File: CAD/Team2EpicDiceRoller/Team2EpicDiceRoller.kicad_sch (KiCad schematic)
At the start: 75 parts, among them J1 Conn_02x03_Odd_Even, J2 Conn_01x16, J3 Barrel_Jack, Q1 BSS138, SW1 SW_Toggle_SPDT, SW2 Tilt_Switch, SW3 SW_Power, SW4 RotaryEncoder_Switch, SW5 SW_LeftMenu, SW6 SW_MidMenu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

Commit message: updated layout, footprints look good
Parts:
- R12, R13: footprint Resistor_SMD:R_1206_3216Metric_Pad1.30x1.75mm_HandSolder -> Resistor_SMD:R_2512_6332Metric_Pad1.40x3.35mm_HandSolder
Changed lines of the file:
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@@
       (effects (font (size 1.27 1.27)) (justify left))
     )
-    (property "Footprint" "Resistor_SMD:R_1206_3216Metric_Pad1.30x1.75mm_HandSolder" (id 2) (at 153.162 179.07 90)
+    (property "Footprint" "Resistor_SMD:R_2512_6332Metric_Pad1.40x3.35mm_HandSolder" (id 2) (at 153.162 179.07 90)
       (effects (font (size 1.27 1.27)) hide)
     )
@@
       (effects (font (size 1.27 1.27)) (justify left))
     )
-    (property "Footprint" "Resistor_SMD:R_1206_3216Metric_Pad1.30x1.75mm_HandSolder" (id 2) (at 154.432 142.24 90)
+    (property "Footprint" "Resistor_SMD:R_2512_6332Metric_Pad1.40x3.35mm_HandSolder" (id 2) (at 154.432 142.24 90)
       (effects (font (size 1.27 1.27)) hide)
     )
@@
     )
     (path "/6b508d04-a0ae-4129-b291-a30a6f3fd6be"
-      (reference "R12") (unit 1) (value "150") (footprint "Resistor_SMD:R_1206_3216Metric_Pad1.30x1.75mm_HandSolder")
+      (reference "R12") (unit 1) (value "150") (footprint "Resistor_SMD:R_2512_6332Metric_Pad1.40x3.35mm_HandSolder")
     )
     (path "/889f4fab-9685-4cef-a698-9695691b09ce"
-      (reference "R13") (unit 1) (value "150") (footprint "Resistor_SMD:R_1206_3216Metric_Pad1.30x1.75mm_HandSolder")
+      (reference "R13") (unit 1) (value "150") (footprint "Resistor_SMD:R_2512_6332Metric_Pad1.40x3.35mm_HandSolder")
     )
     (path "/a2c9735e-4a2d-405c-869d-3d050fdc7cf6"

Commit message: Replaced footprint for 470uF cap
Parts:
- C6, C8: footprint Capacitor_THT:CP_Radial_D5.0mm_P2.50mm -> Capacitor_THT:CP_Radial_D6.3mm_P2.50mm
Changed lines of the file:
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@@
       (effects (font (size 1.27 1.27)) (justify left))
     )
-    (property "Footprint" "Capacitor_THT:CP_Radial_D5.0mm_P2.50mm" (id 2) (at 98.7552 173.99 0)
+    (property "Footprint" "Capacitor_THT:CP_Radial_D6.3mm_P2.50mm" (id 2) (at 98.7552 173.99 0)
       (effects (font (size 1.27 1.27)) hide)
     )
@@
       (effects (font (size 1.27 1.27)) (justify left))
     )
-    (property "Footprint" "Capacitor_THT:CP_Radial_D5.0mm_P2.50mm" (id 2) (at 129.2352 137.16 0)
+    (property "Footprint" "Capacitor_THT:CP_Radial_D6.3mm_P2.50mm" (id 2) (at 129.2352 137.16 0)
       (effects (font (size 1.27 1.27)) hide)
     )
@@
     )
     (path "/5742b5fd-3f8d-4d64-bb1a-04db38f14d1d"
-      (reference "C6") (unit 1) (value "470u") (footprint "Capacitor_THT:CP_Radial_D5.0mm_P2.50mm")
+      (reference "C6") (unit 1) (value "470u") (footprint "Capacitor_THT:CP_Radial_D6.3mm_P2.50mm")
     )
     (path "/e430aba8-016f-47fe-86d9-c150d7f518cd"
@@
     )
     (path "/9c48a684-ed08-4a42-8221-2c4c4eaf77cd"
-      (reference "C8") (unit 1) (value "470u") (footprint "Capacitor_THT:CP_Radial_D5.0mm_P2.50mm")
+      (reference "C8") (unit 1) (value "470u") (footprint "Capacitor_THT:CP_Radial_D6.3mm_P2.50mm")
     )
     (path "/7e5013ac-be8e-44d0-99da-910d44977e25"

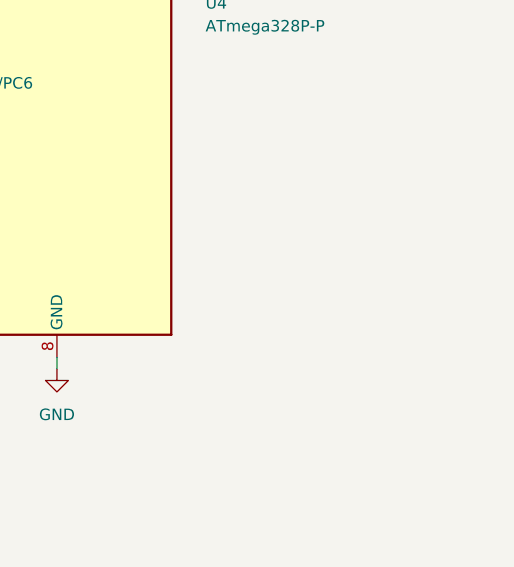
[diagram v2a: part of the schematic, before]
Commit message: Added mounting holes, updated general layout of pcb for routing
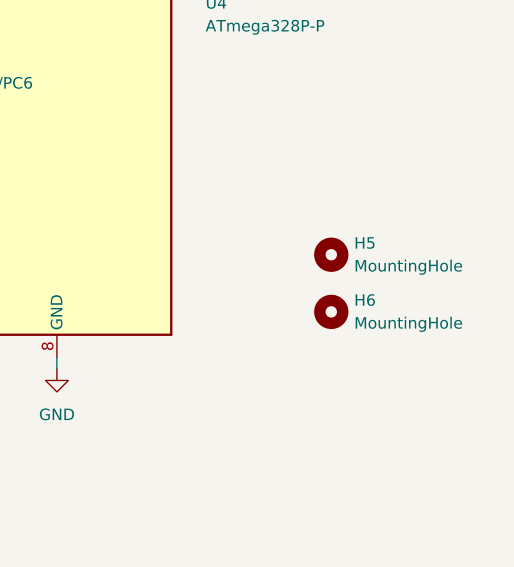
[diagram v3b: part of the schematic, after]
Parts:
- added H5, H6: MountingHole, MountingHole:MountingHole_3.2mm_M3, symbol Mechanical:MountingHole
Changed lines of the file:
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@@
+    )
+  )
+  (symbol (lib_id "Mechanical:MountingHole") (at 267.97 149.86 0) (unit 1)
+    (in_bom yes) (on_board yes) (fields_autoplaced)
+    (property "Reference" "H5" (id 0) (at 270.51 148.5899 0)
+      (effects (font (size 1.27 1.27)) (justify left))
+    )
+    (property "Value" "MountingHole" (id 1) (at 270.51 151.1299 0)
+      (effects (font (size 1.27 1.27)) (justify left))
+    )
+    (property "Footprint" "MountingHole:MountingHole_3.2mm_M3" (id 2) (at 267.97 149.86 0)
+      (effects (font (size 1.27 1.27)) hide)
+    )
+    (property "Datasheet" "~" (id 3) (at 267.97 149.86 0)
+      (effects (font (size 1.27 1.27)) hide)
+    )
+  )
+  (symbol (lib_id "Mechanical:MountingHole") (at 267.97 156.21 0) (unit 1)
+    (in_bom yes) (on_board yes) (fields_autoplaced)
+    (property "Reference" "H6" (id 0) (at 270.51 154.9399 0)
+      (effects (font (size 1.27 1.27)) (justify left))
+    )
+    (property "Value" "MountingHole" (id 1) (at 270.51 157.4799 0)
+      (effects (font (size 1.27 1.27)) (justify left))
+    )
+    (property "Footprint" "MountingHole:MountingHole_3.2mm_M3" (id 2) (at 267.97 156.21 0)
+      (effects (font (size 1.27 1.27)) hide)
+    )
+    (property "Datasheet" "~" (id 3) (at 267.97 156.21 0)
+      (effects (font (size 1.27 1.27)) hide)
     )
   )
@@
       (reference "H4") (unit 1) (value "MountingHole") (footprint "MountingHole:MountingHole_3.2mm_M3")
     )
+    (path "/d0d819c4-15d7-4cc9-a112-ed933c139457"
+      (reference "H5") (unit 1) (value "MountingHole") (footprint "MountingHole:MountingHole_3.2mm_M3")
+    )
+    (path "/ea003e02-1b53-4864-ad7c-936ca22bc3ec"
+      (reference "H6") (unit 1) (value "MountingHole") (footprint "MountingHole:MountingHole_3.2mm_M3")
+    )
     (path "/97500fde-4c78-42dd-ab07-3c6ad623f25a"

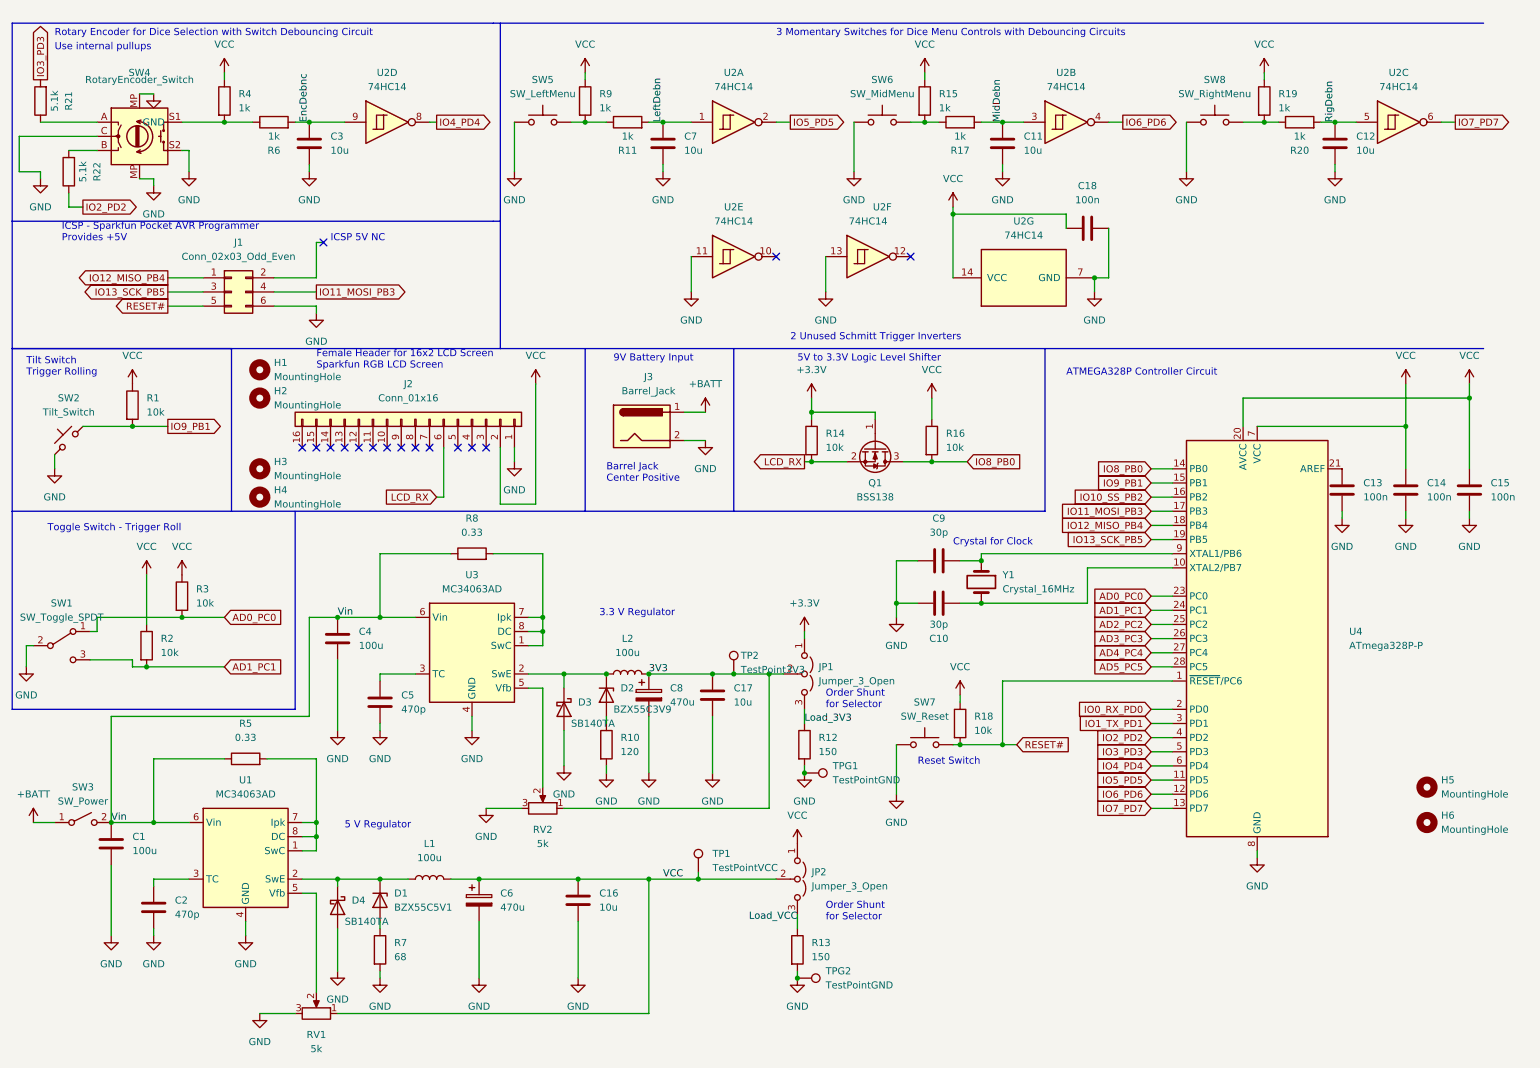
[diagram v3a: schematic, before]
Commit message: Updated pin selections for some of the io so that we can use the screen and the enableinterrupt library at the same time
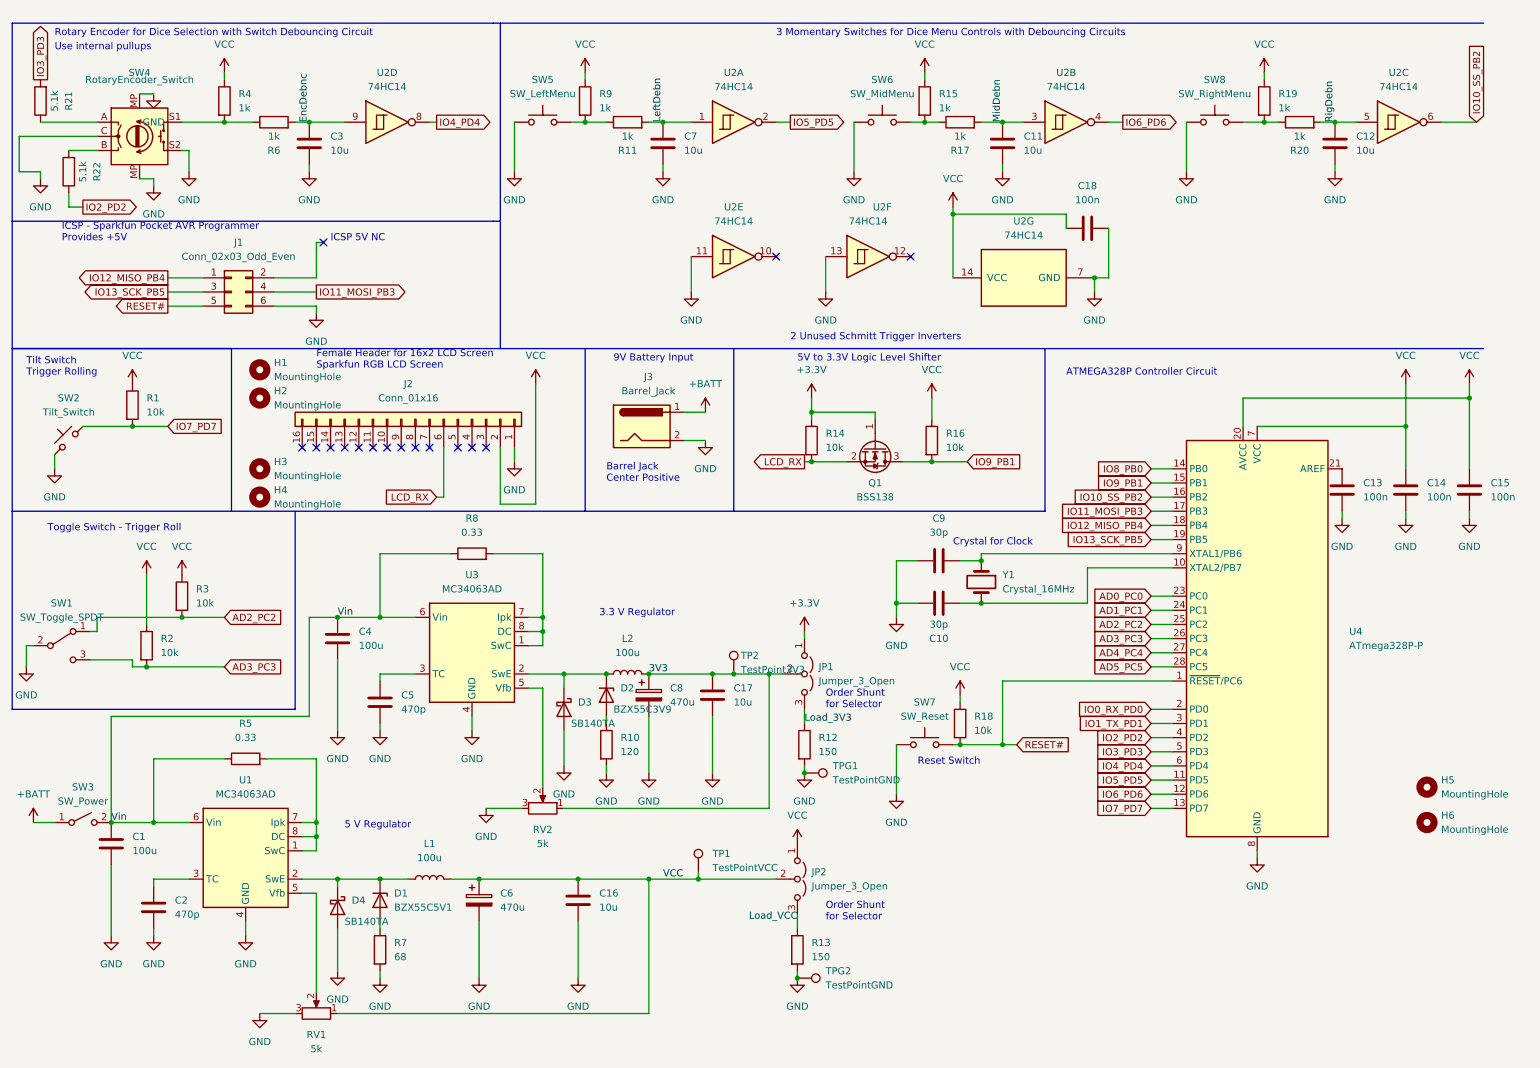
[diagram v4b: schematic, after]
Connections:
- net AD0_PC0: no longer R3.2, SW1.1 (A)
- net AD1_PC1: no longer R2.2, SW1.3 (C)
- net AD2_PC2: now also R3.2, SW1.1 (A)
- net AD3_PC3: now also R2.2, SW1.3 (C)
- net IO10_SS_PB2: now also U2.6
- net IO7_PD7: now also R1.2, SW2.1; no longer U2.6
- net IO8_PB0: no longer Q1.3 (D), R16.2
- net IO9_PB1: now also Q1.3 (D), R16.2; no longer R1.2, SW2.1
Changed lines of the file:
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@@
     (stroke (width 0) (type default) (color 0 0 0 0))
   )
-  (wire (pts (xy 270.51 30.48) (xy 273.05 30.48))
+  (wire (pts (xy 270.51 30.48) (xy 276.86 30.48))
     (stroke (width 0) (type default) (color 0 0 0 0))
   )
@@
     )
   )
-  (global_label "IO9_PB1" (shape output) (at 41.91 85.09 0) (fields_autoplaced)
-    (effects (font (size 1.27 1.27)) (justify left))
-    (property "Intersheet References" "${INTERSHEET_REFS}" (id 0) (at 52.185 85.0106 0)
-      (effects (font (size 1.27 1.27)) (justify left) hide)
-    )
-  )
-  (global_label "AD0_PC0" (shape input) (at 52.07 119.38 0) (fields_autoplaced)
-    (effects (font (size 1.27 1.27)) (justify left))
-    (property "Intersheet References" "${INTERSHEET_REFS}" (id 0) (at 62.7683 119.3006 0)
-      (effects (font (size 1.27 1.27)) (justify left) hide)
-    )
-  )
-  (global_label "AD1_PC1" (shape input) (at 52.07 128.27 0) (fields_autoplaced)
-    (effects (font (size 1.27 1.27)) (justify left))
-    (property "Intersheet References" "${INTERSHEET_REFS}" (id 0) (at 62.7683 128.1906 0)
+  (global_label "IO7_PD7" (shape input) (at 41.91 85.09 0) (fields_autoplaced)
+    (effects (font (size 1.27 1.27)) (justify left))
+    (property "Intersheet References" "${INTERSHEET_REFS}" (id 0) (at 52.185 85.1694 0)
+      (effects (font (size 1.27 1.27)) (justify left) hide)
+    )
+  )
+  (global_label "AD2_PC2" (shape input) (at 52.07 119.38 0) (fields_autoplaced)
+    (effects (font (size 1.27 1.27)) (justify left))
+    (property "Intersheet References" "${INTERSHEET_REFS}" (id 0) (at 62.7683 119.4594 0)
+      (effects (font (size 1.27 1.27)) (justify left) hide)
+    )
+  )
+  (global_label "AD3_PC3" (shape input) (at 52.07 128.27 0) (fields_autoplaced)
+    (effects (font (size 1.27 1.27)) (justify left))
+    (property "Intersheet References" "${INTERSHEET_REFS}" (id 0) (at 62.7683 128.3494 0)
       (effects (font (size 1.27 1.27)) (justify left) hide)
     )
@@
     )
   )
-  (global_label "IO8_PB0" (shape input) (at 185.42 91.44 0) (fields_autoplaced)
+  (global_label "IO9_PB1" (shape input) (at 185.42 91.44 0) (fields_autoplaced)
     (effects (font (size 1.27 1.27)) (justify left))
     (property "Intersheet References" "${INTERSHEET_REFS}" (id 0) (at 195.695 91.5194 0)
@@
     )
   )
-  (global_label "IO7_PD7" (shape output) (at 273.05 30.48 0) (fields_autoplaced)
-    (effects (font (size 1.27 1.27)) (justify left))
-    (property "Intersheet References" "${INTERSHEET_REFS}" (id 0) (at 283.325 30.4006 0)
-      (effects (font (size 1.27 1.27)) (justify left) hide)
-    )
+  (global_label "IO10_SS_PB2" (shape input) (at 276.86 30.48 90) (fields_autoplaced)
+    (effects (font (size 1.27 1.27)) (justify left))
+    (property "Intersheet References" "${INTERSHEET_REFS}" (id 0) (at 276.9394 15.6088 90)
+      (effects (font (size 1.27 1.27)) (justify left) hide)
+    )

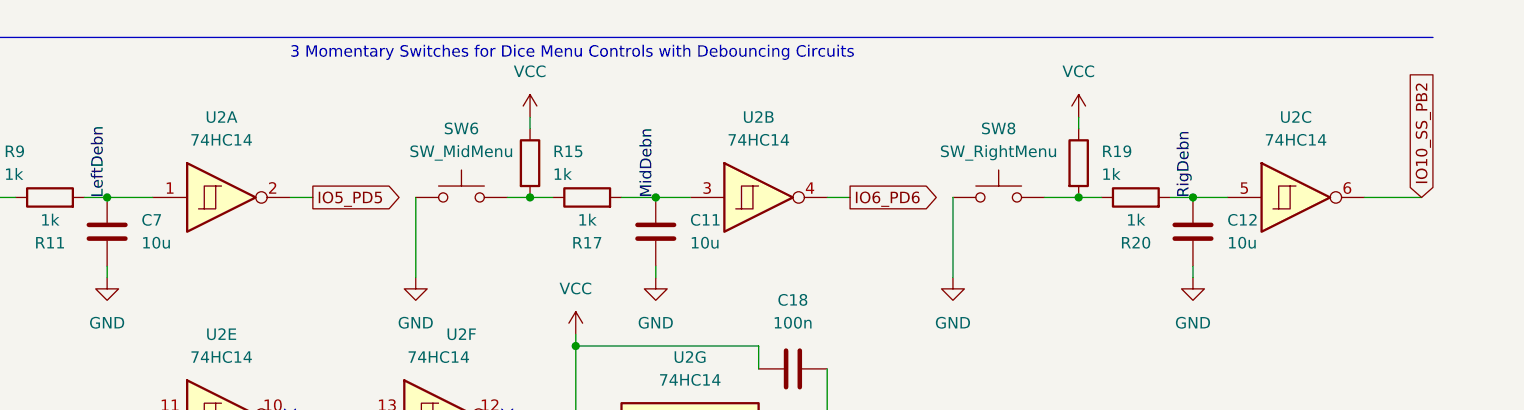
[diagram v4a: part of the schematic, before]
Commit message: Added date to pcb
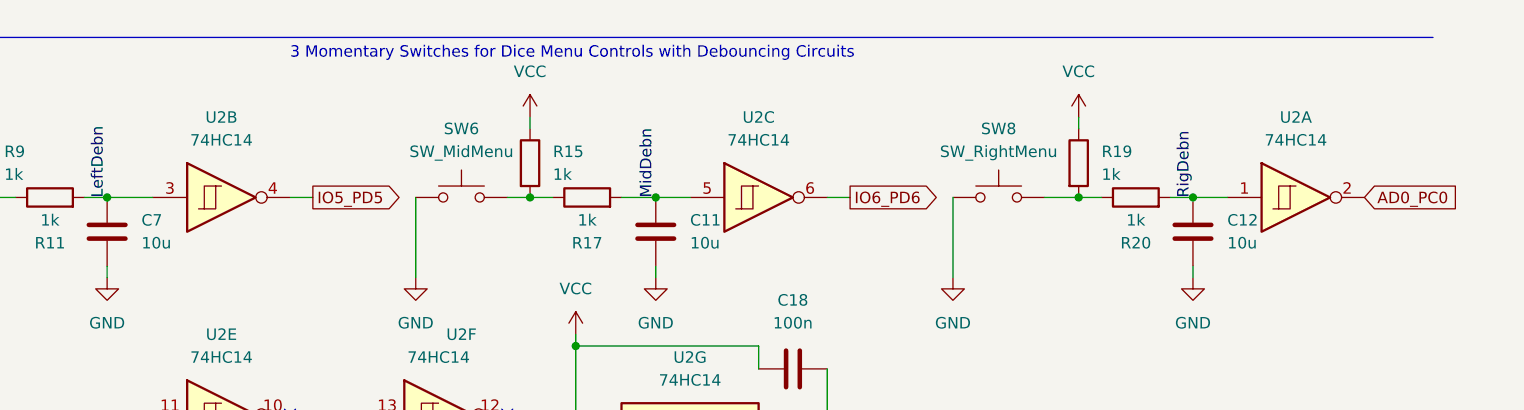
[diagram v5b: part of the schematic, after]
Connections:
- net AD0_PC0: now also U2.2
- net IO10_SS_PB2: no longer U2.6
- net IO5_PD5: now also U2.4; no longer U2.2
- net IO6_PD6: now also U2.6; no longer U2.4
- net LeftDebn: now also U2.3; no longer U2.1
- net MidDebn: now also U2.5; no longer U2.3
- net RigDebn: now also U2.1; no longer U2.5
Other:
- moved on the sheet: U2A, U2B, U2C
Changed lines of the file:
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@@
-    (stroke (width 0) (type default) (color 0 0 0 0))
-  )
-  (wire (pts (xy 270.51 30.48) (xy 276.86 30.48))
     (stroke (width 0) (type default) (color 0 0 0 0))
   )
@@
     )
   )
-  (global_label "IO10_SS_PB2" (shape input) (at 276.86 30.48 90) (fields_autoplaced)
+  (global_label "AD0_PC0" (shape input) (at 270.51 30.48 0) (fields_autoplaced)
     (effects (font (size 1.27 1.27)) (justify left))
-    (property "Intersheet References" "${INTERSHEET_REFS}" (id 0) (at 276.9394 15.6088 90)
+    (property "Intersheet References" "${INTERSHEET_REFS}" (id 0) (at 281.2083 30.5594 0)
       (effects (font (size 1.27 1.27)) (justify left) hide)
     )
@@
     (pin "9")
   )
-  (symbol (lib_id "74xx:74HC14") (at 143.51 30.48 0) (unit 1)
+  (symbol (lib_id "74xx:74HC14") (at 143.51 30.48 0) (unit 2)
     (in_bom yes) (on_board yes) (fields_autoplaced)
     (property "Reference" "U2" (id 0) (at 143.51 21.59 0))
@@
       (effects (font (size 1.27 1.27)) hide)
     )
-    (pin "1")
-    (pin "2")
+    (pin "3")
+    (pin "4")
   )
   (symbol (lib_id "74xx:74HC14") (at 143.51 54.61 0) (unit 5)
@@
     (pin "13")
   )
-  (symbol (lib_id "74xx:74HC14") (at 203.2 30.48 0) (unit 2)
+  (symbol (lib_id "74xx:74HC14") (at 203.2 30.48 0) (unit 3)
     (in_bom yes) (on_board yes) (fields_autoplaced)
     (property "Reference" "U2" (id 0) (at 203.2 21.59 0))
@@
       (effects (font (size 1.27 1.27)) hide)
     )
-    (pin "3")
-    (pin "4")
-  )
-  (symbol (lib_id "74xx:74HC14") (at 262.89 30.48 0) (unit 3)
+    (pin "5")
+    (pin "6")
+  )
+  (symbol (lib_id "74xx:74HC14") (at 262.89 30.48 0) (unit 1)
     (in_bom yes) (on_board yes) (fields_autoplaced)
     (property "Reference" "U2" (id 0) (at 262.89 21.59 0))
@@
       (effects (font (size 1.27 1.27)) hide)
     )
-    (pin "5")
-    (pin "6")
+    (pin "1")
+    (pin "2")
   )
   (symbol (lib_name "RotaryEncoder_Switch_1") (lib_id "Device:RotaryEncoder_Switch") (at 36.83 33.02 0) (unit 1)
